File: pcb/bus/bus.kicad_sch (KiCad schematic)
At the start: 7 parts, among them U101 USBLC6-2SC6, U102 FE1.1s, Y101 12MHz

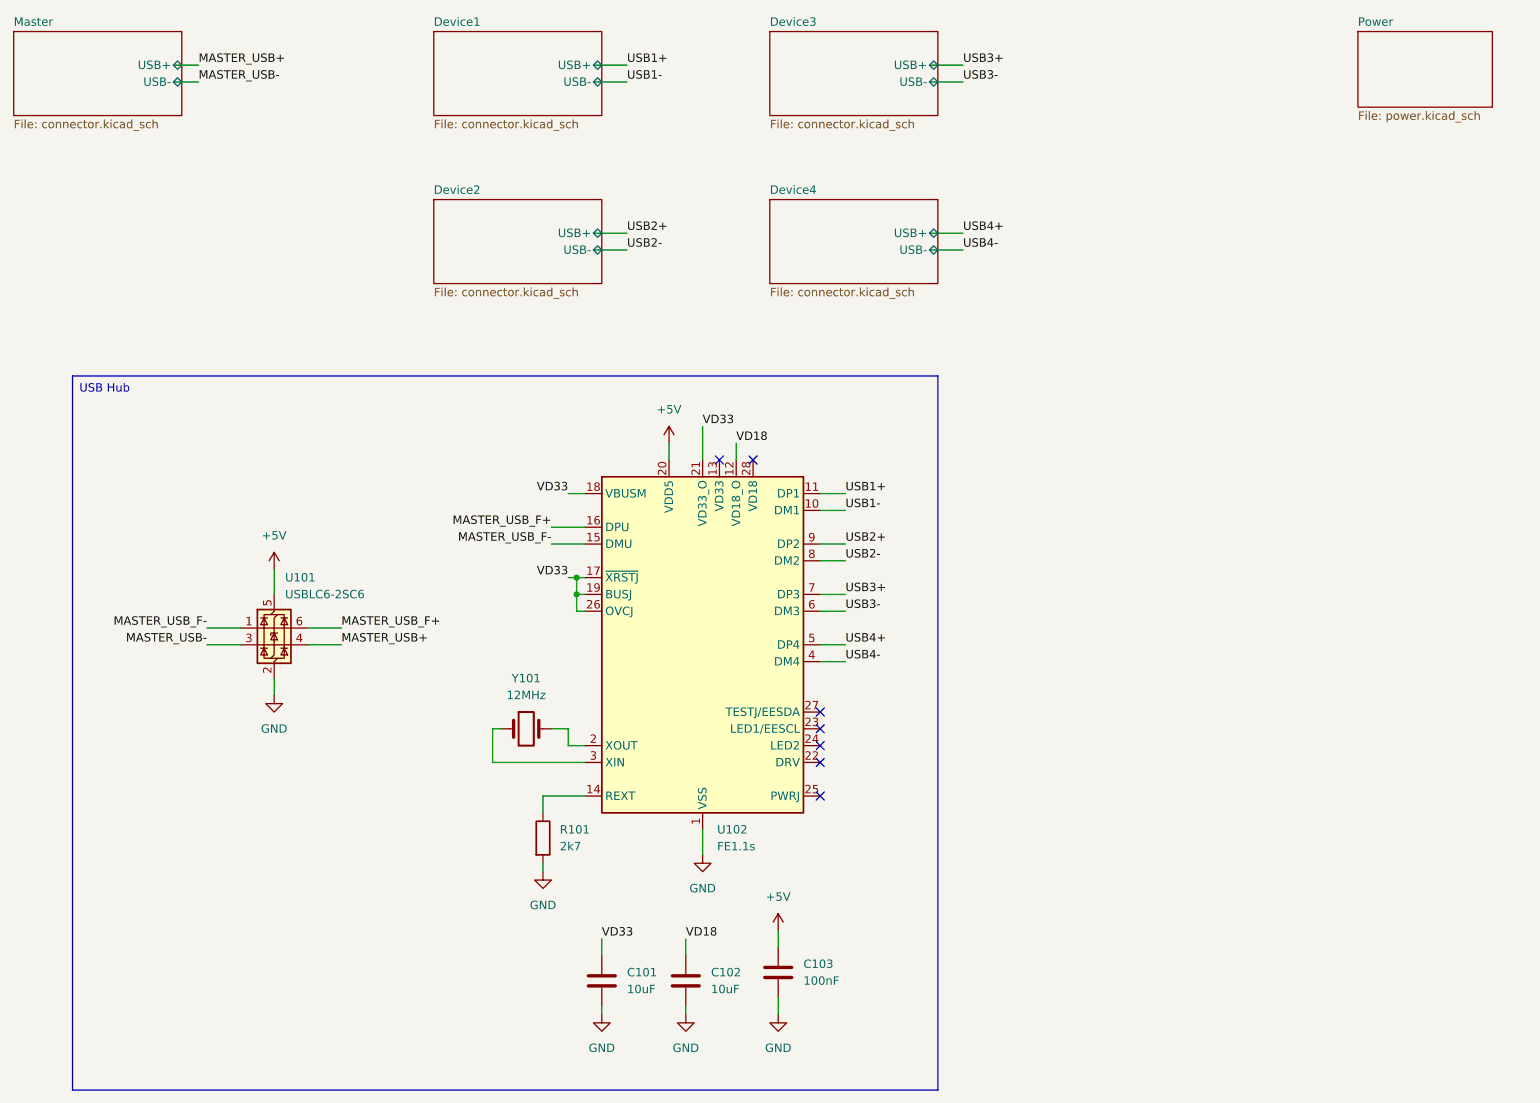
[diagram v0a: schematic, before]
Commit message: update bus schematic
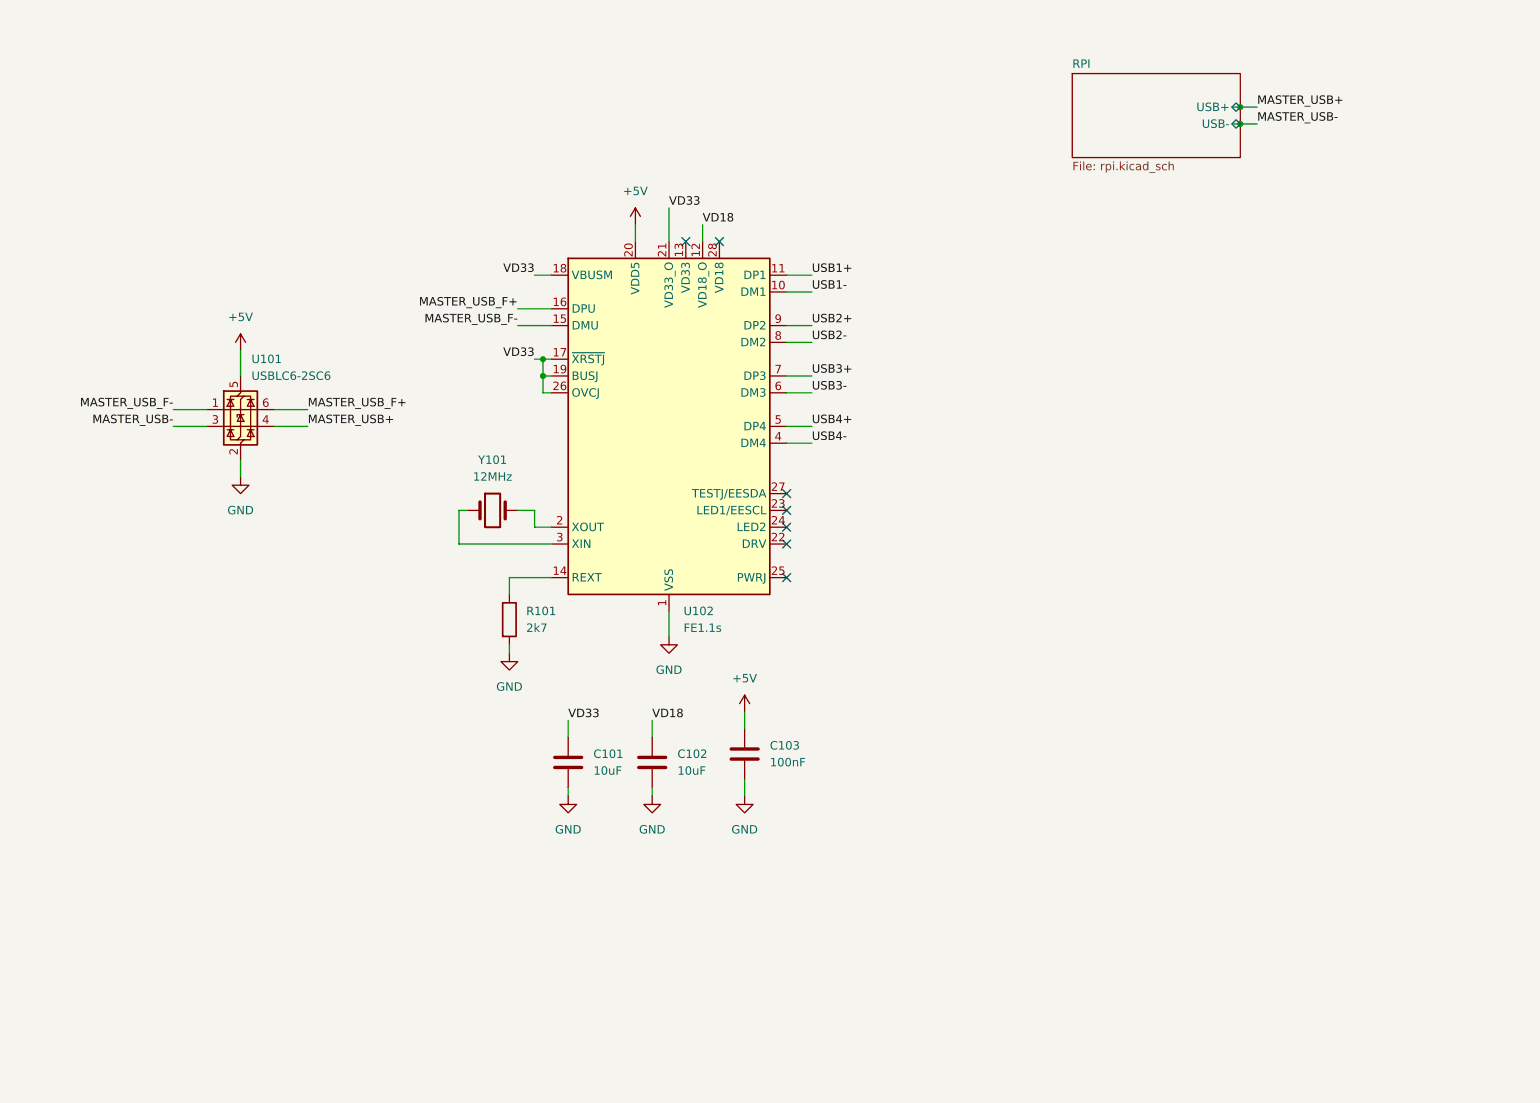
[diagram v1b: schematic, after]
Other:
- sheet Master renamed RPI
- removed sheet Device1
- removed sheet Device2
- removed sheet Device3
- removed sheet Device4
- removed sheet Power
- sheet RPI: file connector.kicad_sch -> rpi.kicad_sch
- moved on the sheet: C101, C102, C103, R101, U101, U102, Y101
